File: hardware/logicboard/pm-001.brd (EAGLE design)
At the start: 45 x 45 mm, 17 parts, among them K1 G5V1, T1 2SC1815

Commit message: Moved the processor slightly so that FTDI adapter easily fits.
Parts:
- moved D2 1.27 mm to (12.7, 2.54)
- moved R2 1.27 mm to (21.6, 2.54)
- moved T1 1.27 mm to (29.2, 2.54)
- moved U$1 1.27 mm to (26.7, 21.6)
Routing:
- net VIN: track 40.3 -> 53.1 mm
- net VCC: track 92.4 -> 87.0 mm
- net GND: track 79.0 -> 81.5 mm
- net N$5: track 53.9 -> 52.0 mm
- net N$9: track 3.81 -> 5.08 mm
- net N$16: track 3.81 -> 5.08 mm
- net N$15: track 3.81 -> 5.08 mm
- net N$14: track 3.81 -> 5.08 mm
- net N$13: track 3.81 -> 5.08 mm
- net N$12: track 3.81 -> 5.08 mm
- net N$8: track 27.1 -> 28.1 mm
- net N$11: track 27.1 -> 26.3 mm
- net N$10: track 18.0 -> 17.3 mm
- net N$3: track 6.66 -> 6.13 mm
- net IND: track 25.3 -> 25.9 mm

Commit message: D8 -> D2.
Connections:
- net N$7: now also U$1.D2; no longer U$1.D8
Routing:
- net N$7: track 7.30 -> 22.5 mm
- net VIN: track 53.1 -> 40.9 mm
- net VCC: track 87.0 -> 94.6 mm
- net N$5: track 52.0 -> 56.0 mm

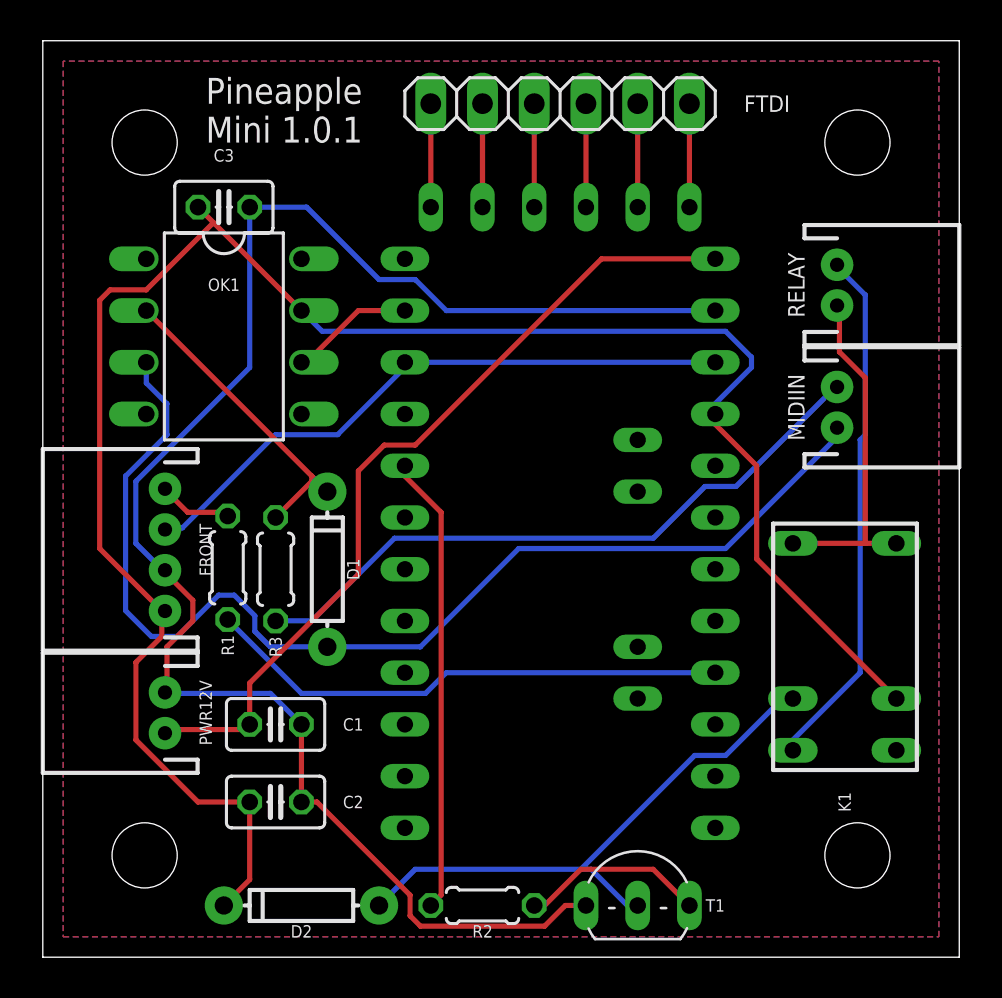
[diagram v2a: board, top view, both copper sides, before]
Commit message: Sockets for stacking.
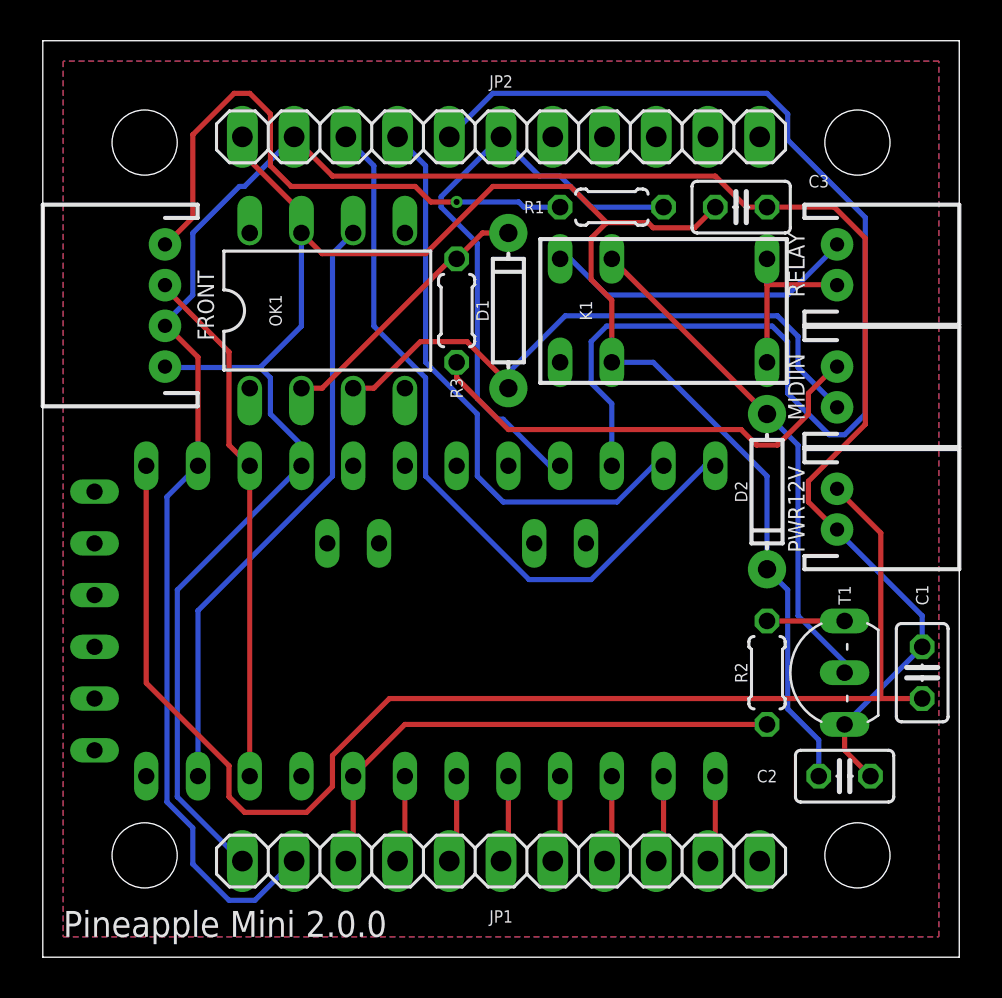
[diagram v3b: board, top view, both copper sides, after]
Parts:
- removed FTDI: (no value), pinhead:1X06
- added JP1, JP2: (no value), pinhead:1X11
- moved PWR12V 34.5 mm to (39.0, 22.0), turned to 270 degrees
- moved C1 31.9 mm to (43.2, 14.0), turned to 90 degrees
- moved D2 30.6 mm to (35.6, 22.9), turned to 270 degrees
- moved C2 28.0 mm to (39.4, 8.89)
- moved R1 25.9 mm to (27.9, 36.8), turned to 0 degrees
- moved C3 25.4 mm to (34.3, 36.8)
- moved K1 18.8 mm to (30.5, 31.8), turned to 0 degrees
- moved R2 18.1 mm to (35.6, 14.0), turned to 90 degrees
- moved D1 15.5 mm to (22.9, 31.8)
- moved R3 15.5 mm to (20.3, 31.8)
- moved T1 15.3 mm to (39.4, 14.0), turned to 90 degrees
- moved FRONT 12.0 mm to (6.00, 32.0)
- moved U$1 9.67 mm to (17.8, 17.8), turned to 90 degrees
- moved OK1 5.24 mm to (14.0, 31.8), turned to 0 degrees
- moved MIDIIN 1.00 mm to (39.0, 28.0)
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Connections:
- removed net IND: R1.2, U$1.D13
- removed net N$12: FTDI.2, U$1.GND3
- removed net N$13: FTDI.3, U$1.VCC1
- removed net N$14: FTDI.4, U$1.RX1-1
- removed net N$15: FTDI.5, U$1.TX0-1
- removed net N$16: FTDI.6, U$1.DTR
- removed net N$7: R2.1, U$1.D2
- removed net N$9: FTDI.1, U$1.GND2
- new net 0: JP1.3, R2.1, U$1.D2
- new net 1: JP1.4, U$1.D3
- new net 10: JP2.5, U$1.D12
- new net 11: JP2.6, R1.2, U$1.D13
- new net 2: JP1.5, U$1.D4
- new net 3: JP1.6, U$1.D5
- new net 4: JP1.7, U$1.D6
- new net 5: JP1.8, U$1.D7
- new net 6: JP1.9, U$1.D8
- new net 7: JP1.10, U$1.D9
- new net 8: JP2.3, U$1.D10
- new net 9: JP2.4, U$1.D11
- net GND: now also JP1.2, JP2.2
- net VCC: now also JP1.1, JP2.1
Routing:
- net 10: track 0.00 -> 58.6 mm
- net 8: track 0.00 -> 36.9 mm
- net 11: track 0.00 -> 29.7 mm
- net 9: track 0.00 -> 28.7 mm
- net GND: track 81.5 -> 109.0 mm
- net IND: track 25.9 -> 0.00 mm
- net VIN: track 40.9 -> 66.7 mm
- net 0: track 0.00 -> 25.7 mm
- net N$5: track 56.0 -> 30.5 mm
- net N$1: track 3.65 -> 28.6 mm, vias 0 -> 1
- net N$3: track 6.13 -> 29.8 mm
- net N$7: track 22.5 -> 0.00 mm
- net N$11: track 25.9 -> 15.4 mm
- net N$2: track 32.3 -> 23.0 mm
- net VCC: track 94.6 -> 103.7 mm
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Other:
- board text added: "Pineapple Mini 2.0.0"
- board text removed: "Pineapple Mini 1.0.1"
